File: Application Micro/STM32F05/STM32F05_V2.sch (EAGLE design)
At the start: 46 parts, among them T1 FDN340P, T2 AP1117_LIN_REG

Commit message: Application Micro V2
Removed shift regulator (for I2C), named pins, connected can circuit to
can schematic.
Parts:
- removed BSS138: n-chanel mosfet, DiscreteComponents:BSS138
- removed R10, R11, R12, R9: 10K, rcl:R-US_R0603
- removed U$6: BSS138, DiscreteComponents:BSS138
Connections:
- net PIN22 renamed CAM_LED
- net PIN58 renamed TEMP_SENS
- net PIN8 renamed SHFT_REG_DATA
- removed net PIN10: SV1.9, U$1G$3.PC2
- removed net PIN33: SV4.1, U$1G$2.PB12
- removed net PIN34: SV4.2, U$1G$2.PB13
- removed net PIN37: SV4.5, U$1G$3.PC6
- removed net PIN38: SV4.6, U$1G$3.PC7
- removed net PIN39: SV4.7, U$1G$3.PC8
- removed net PIN40: SV4.8, U$1G$3.PC9
- removed net PIN44: SV4.12, U$1G$1.PA11
- removed net PIN9: SV1.10, U$1G$3.PC1
- removed net RXD: U$5.RXD
- removed net SCL1: BSS138.S, R11.1
- removed net SCL2: BSS138.D, R9.1
- removed net SDA1: R12.1, U$6.S
- removed net SDA2: R10.1, U$6.D
- removed net TXD: U$5.TXD
- new net CAN2_RX: SV4.1, U$1G$2.PB12, U$5.RXD
- new net CAN2_TX: SV4.2, U$1G$2.PB13, U$5.TXD
- new net DBUG_LED1: R3.2, SV4.8, U$1G$3.PC9
- new net DBUG_LED2: R4.2, SV4.7, U$1G$3.PC8
- new net DBUG_LED3: R5.2, SV4.6, U$1G$3.PC7
- new net DBUG_LED4: R6.2, SV4.5, U$1G$3.PC6
- new net SHFT_REG_CLK: SV1.9, U$1G$3.PC1
- new net SHFT_REG_EN: SV1.10, U$1G$3.PC2
- net +3V3: no longer BSS138.G, R11.2, R12.2, U$6.G
- net +5V: no longer R10.2, R9.2
- net PIN43: no longer SV4.11
- net PIN45: no longer U$1G$1.PA12
- net USBD+: now also SV4.12, U$1G$1.PA12
- net USBD-: now also SV4.11, U$1G$1.PA11
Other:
- note removed: "Bi-Directional Level Shifter"
- moved on the sheet: ASV, C11, C7, R1, R2, SV2, SV4

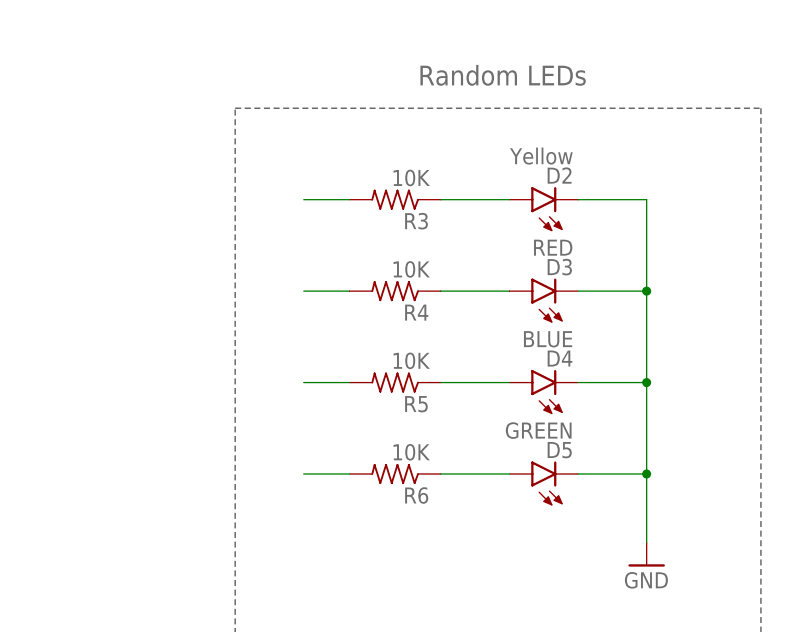
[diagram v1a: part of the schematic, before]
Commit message: change the value of LED resistors
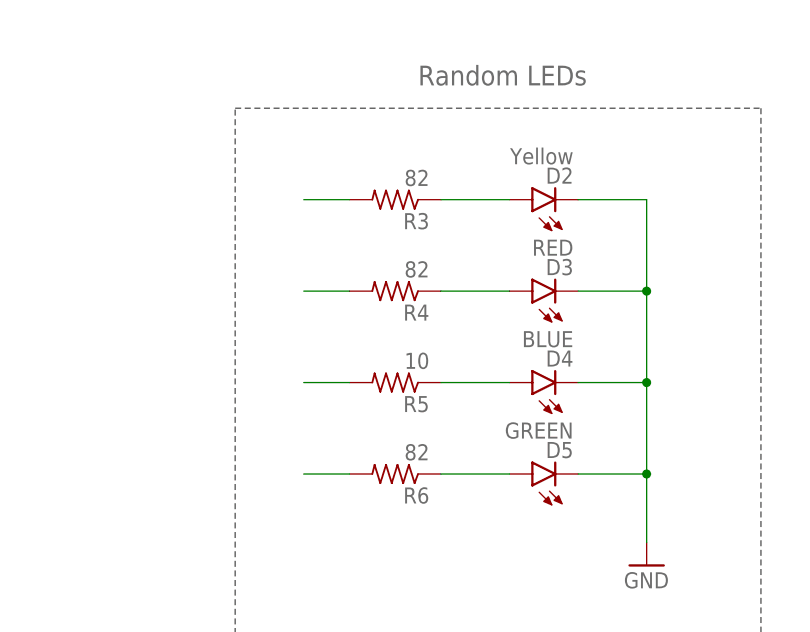
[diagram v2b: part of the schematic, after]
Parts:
- R3, R4, R6: value 10K -> 82
- R5: value 10K -> 10
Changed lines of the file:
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@@
 <?xml version="1.0" encoding="utf-8"?>
 <!DOCTYPE eagle SYSTEM "eagle.dtd">
-<eagle version="7.5.0">
+<eagle version="7.4.0">
 <drawing>
 <settings>
@@
 <part name="D4" library="SparkFun-LED" deviceset="LED-BLUE" device="0603" value="BLUE"/>
 <part name="D5" library="SparkFun-LED" deviceset="LED-GREEN" device="0603" value="GREEN"/>
-<part name="R3" library="rcl" deviceset="R-US_" device="R0603" value="10K"/>
-<part name="R4" library="rcl" deviceset="R-US_" device="R0603" value="10K"/>
-<part name="R5" library="rcl" deviceset="R-US_" device="R0603" value="10K"/>
-<part name="R6" library="rcl" deviceset="R-US_" device="R0603" value="10K"/>
+<part name="R3" library="rcl" deviceset="R-US_" device="R0603" value="82"/>
+<part name="R4" library="rcl" deviceset="R-US_" device="R0603" value="82"/>
+<part name="R5" library="rcl" deviceset="R-US_" device="R0603" value="10"/>
+<part name="R6" library="rcl" deviceset="R-US_" device="R0603" value="82"/>
 <part name="GND7" library="supply1" deviceset="GND" device=""/>
 <part name="U$5" library="MAX3051 Library" deviceset="MAX3051" device="MAX3051"/>
